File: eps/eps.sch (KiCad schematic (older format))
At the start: 64 parts, among them Q1 IRF7404, Q10 2N7002, Q11 IRF7404, Q12 2N7002, Q13 IRF7404, Q14 2N7002, Q15 IRF7404, Q16 IRF7404, Q17 IRF7404, Q18 IRF7404, Q19 IRF7404, Q2 2N7002, Q20 2N7002, Q21 IRF7404, Q22 2N7002, Q23 IRF7404, Q24 2N7002, Q3 IRF7404, Q4 2N7002, Q5 IRF7404, Q6 2N7002, Q7 IRF7404, Q8 2N7002, Q9 IRF7404

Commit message: switching regs
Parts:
- added U?: ADP2303ARDZ-3.3, Package_SO:SOIC-8-1EP_3.9x4.9mm_P1.27mm_EP2.29x3mm, symbol Regulator_Switching:ADP2303ARDZ-3.3
- added U?: ADP2303ARDZ-5.0, Package_SO:SOIC-8-1EP_3.9x4.9mm_P1.27mm_EP2.29x3mm, symbol Regulator_Switching:ADP2303ARDZ-5.0
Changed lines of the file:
@@
+	1    0    0    -1
+$EndComp
+$Comp
+L Regulator_Switching:ADP2303ARDZ-3.3 U?
+U 1 1 61773BE3
+P 6700 4800
+F 0 "U?" H 6700 5267 50  0000 C CNN
+F 1 "ADP2303ARDZ-3.3" H 6700 5176 50  0000 C CNN
+F 2 "Package_SO:SOIC-8-1EP_3.9x4.9mm_P1.27mm_EP2.29x3mm" H 6850 4450 50  0001 L CNN
+F 3 "https://www.analog.com/media/en/technical-documentation/data-sheets/ADP2302_2303.pdf" H 6500 5400 50  0001 C CNN
+	1    6700 4800
+	1    0    0    -1
+$EndComp
+$Comp
+L Regulator_Switching:ADP2303ARDZ-5.0 U?
+U 1 1 61775A47
+P 8750 4900
+F 0 "U?" H 8750 5367 50  0000 C CNN
+F 1 "ADP2303ARDZ-5.0" H 8750 5276 50  0000 C CNN
+F 2 "Package_SO:SOIC-8-1EP_3.9x4.9mm_P1.27mm_EP2.29x3mm" H 8900 4550 50  0001 L CNN
+F 3 "https://www.analog.com/media/en/technical-documentation/data-sheets/ADP2302_2303.pdf" H 8550 5500 50  0001 C CNN
+	1    8750 4900
 	1    0    0    -1
 $EndComp

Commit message: switching regulators
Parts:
- removed U?: ADP2303ARDZ-3.3, Package_SO:SOIC-8-1EP_3.9x4.9mm_P1.27mm_EP2.29x3mm, symbol Regulator_Switching:ADP2303ARDZ-3.3
- added U1: ADP2302ARDZ-3.3, Package_SO:SOIC-8-1EP_3.9x4.9mm_P1.27mm_EP2.29x3mm, symbol Regulator_Switching:ADP2302ARDZ-3.3
- added U3: CS5172EDR8G, symbol epslib:CS5172EDR8G
- gave numbers to parts that had none: 1
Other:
- moved on the sheet: U2
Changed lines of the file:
@@
 	1700 4200 2500 4200
 $Comp
-L power:GND #PWR?
+L power:GND #PWR0101
 U 1 1 617757AB
 P 2500 4200
-F 0 "#PWR?" H 2500 3950 50  0001 C CNN
+F 0 "#PWR0101" H 2500 3950 50  0001 C CNN
 F 1 "GND" H 2505 4027 50  0000 C CNN
 F 2 "" H 2500 4200 50  0001 C CNN
@@
 BUS12SIG
 $Comp
-L power:+12V #PWR?
+L power:+12V #PWR0102
 U 1 1 61798D3E
 P 9450 2900
-F 0 "#PWR?" H 9450 2750 50  0001 C CNN
+F 0 "#PWR0102" H 9450 2750 50  0001 C CNN
 F 1 "+12V" V 9465 3028 50  0000 L CNN
 F 2 "" H 9450 2900 50  0001 C CNN
@@
 $EndComp
 $Comp
-L power:+3.3V #PWR?
+L power:+3.3V #PWR0103
 U 1 1 6179B4E0
 P 4800 2900
-F 0 "#PWR?" H 4800 2750 50  0001 C CNN
+F 0 "#PWR0103" H 4800 2750 50  0001 C CNN
 F 1 "+3.3V" V 4815 3028 50  0000 L CNN
 F 2 "" H 4800 2900 50  0001 C CNN
@@
 $EndComp
 $Comp
-L power:+12V #PWR?
+L power:+12V #PWR0104
 U 1 1 6179E69D
 P 4800 800
-F 0 "#PWR?" H 4800 650 50  0001 C CNN
+F 0 "#PWR0104" H 4800 650 50  0001 C CNN
 F 1 "+12V" V 4815 928 50  0000 L CNN
 F 2 "" H 4800 800 50  0001 C CNN
@@
 BUSBSIG
 $Comp
-L power:+3.3V #PWR?
+L power:+3.3V #PWR0105
 U 1 1 617A7227
 P 7900 1850
-F 0 "#PWR?" H 7900 1700 50  0001 C CNN
+F 0 "#PWR0105" H 7900 1700 50  0001 C CNN
 F 1 "+3.3V" V 7915 1978 50  0000 L CNN
 F 2 "" H 7900 1850 50  0001 C CNN
@@
 $EndComp
 $Comp
-L power:+BATT #PWR?
+L power:+BATT #PWR0106
 U 1 1 617A95E4
 P 7900 2900
-F 0 "#PWR?" H 7900 2750 50  0001 C CNN
+F 0 "#PWR0106" H 7900 2750 50  0001 C CNN
 F 1 "+BATT" H 7915 3073 50  0000 C CNN
 F 2 "" H 7900 2900 50  0001 C CNN
@@
 	4350 800  4800 800
 $Comp
-L power:GND #PWR?
+L power:GND #PWR0107
 U 1 1 617E29A2
 P 4350 1600
-F 0 "#PWR?" H 4350 1350 50  0001 C CNN
+F 0 "#PWR0107" H 4350 1350 50  0001 C CNN
 F 1 "GND" H 4355 1427 50  0000 C CNN
 F 2 "" H 4350 1600 50  0001 C CNN
@@
 SIG2
 $Comp
-L power:+12V #PWR?
+L power:+12V #PWR0108
 U 1 1 617F4B03
 P 6350 800
-F 0 "#PWR?" H 6350 650 50  0001 C CNN
+F 0 "#PWR0108" H 6350 650 50  0001 C CNN
 F 1 "+12V" V 6365 928 50  0000 L CNN
 F 2 "" H 6350 800 50  0001 C CNN
@@
 	5900 800  6350 800
 $Comp
-L power:GND #PWR?
+L power:GND #PWR0109
 U 1 1 617F4B27
 P 5900 1600
-F 0 "#PWR?" H 5900 1350 50  0001 C CNN
+F 0 "#PWR0109" H 5900 1350 50  0001 C CNN
 F 1 "GND" H 5905 1427 50  0000 C CNN
 F 2 "" H 5900 1600 50  0001 C CNN
@@
 	7450 800  7900 800
 $Comp
-L power:GND #PWR?
+L power:GND #PWR0110
 U 1 1 6180AD18
 P 7450 1600
-F 0 "#PWR?" H 7450 1350 50  0001 C CNN
+F 0 "#PWR0110" H 7450 1350 50  0001 C CNN
 F 1 "GND" H 7455 1427 50  0000 C CNN
 F 2 "" H 7450 1600 50  0001 C CNN
@@
 	7100 1300 7150 1300
 $Comp
-L power:+BATT #PWR?
+L power:+BATT #PWR0111
 U 1 1 6180E8E3
 P 7900 800
-F 0 "#PWR?" H 7900 650 50  0001 C CNN
+F 0 "#PWR0111" H 7900 650 50  0001 C CNN
 F 1 "+BATT" H 7915 973 50  0000 C CNN
 F 2 "" H 7900 800 50  0001 C CNN
@@
 	9000 800  9450 800
 $Comp
-L power:GND #PWR?
+L power:GND #PWR0112
 U 1 1 6182C3CE
 P 9000 1600
-F 0 "#PWR?" H 9000 1350 50  0001 C CNN
+F 0 "#PWR0112" H 9000 1350 50  0001 C CNN
 F 1 "GND" H 9005 1427 50  0000 C CNN
 F 2 "" H 9000 1600 50  0001 C CNN
@@
 	8650 1300 8700 1300
 $Comp
-L power:+BATT #PWR?
+L power:+BATT #PWR0113
 U 1 1 6182C3E0
 P 9450 800
-F 0 "#PWR?" H 9450 650 50  0001 C CNN
+F 0 "#PWR0113" H 9450 650 50  0001 C CNN
 F 1 "+BATT" H 9465 973 50  0000 C CNN
 F 2 "" H 9450 800 50  0001 C CNN
@@
 	10550 800  11000 800
 $Comp
-L power:GND #PWR?
+L power:GND #PWR0114
 U 1 1 61857DDD
 P 10550 1600
-F 0 "#PWR?" H 10550 1350 50  0001 C CNN
+F 0 "#PWR0114" H 10550 1350 50  0001 C CNN
 F 1 "GND" H 10555 1427 50  0000 C CNN
 F 2 "" H 10550 1600 50  0001 C CNN
@@
 	10200 1300 10250 1300
 $Comp
-L power:+5V #PWR?
+L power:+5V #PWR0115
 U 1 1 6185C627
 P 11000 800
-F 0 "#PWR?" H 11000 650 50  0001 C CNN
+F 0 "#PWR0115" H 11000 650 50  0001 C CNN
 F 1 "+5V" V 11015 928 50  0000 L CNN
 F 2 "" H 11000 800 50  0001 C CNN
@@
 	4350 1850 4800 1850
 $Comp
-L power:GND #PWR?
+L power:GND #PWR0116
 U 1 1 61868CA2
 P 4350 2650
-F 0 "#PWR?" H 4350 2400 50  0001 C CNN
+F 0 "#PWR0116" H 4350 2400 50  0001 C CNN
 F 1 "GND" H 4355 2477 50  0000 C CNN
 F 2 "" H 4350 2650 50  0001 C CNN
@@
 	4000 2350 4050 2350
 $Comp
-L power:+5V #PWR?
+L power:+5V #PWR0117
 U 1 1 61868CB4
 P 4800 1850
-F 0 "#PWR?" H 4800 1700 50  0001 C CNN
+F 0 "#PWR0117" H 4800 1700 50  0001 C CNN
 F 1 "+5V" V 4815 1978 50  0000 L CNN
 F 2 "" H 4800 1850 50  0001 C CNN
@@
 	5900 1850 6350 1850
 $Comp
-L power:GND #PWR?
+L power:GND #PWR0118
 U 1 1 61889281
 P 5900 2650
-F 0 "#PWR?" H 5900 2400 50  0001 C CNN
+F 0 "#PWR0118" H 5900 2400 50  0001 C CNN
 F 1 "GND" H 5905 2477 50  0000 C CNN
 F 2 "" H 5900 2650 50  0001 C CNN
@@
 	5550 2350 5600 2350
 $Comp
-L power:+5V #PWR?
+L power:+5V #PWR0119
 U 1 1 61889293
 P 6350 1850
-F 0 "#PWR?" H 6350 1700 50  0001 C CNN
+F 0 "#PWR0119" H 6350 1700 50  0001 C CNN
 F 1 "+5V" V 6365 1978 50  0000 L CNN
 F 2 "" H 6350 1850 50  0001 C CNN
@@
 Connection ~ 7900 1850
 $Comp
-L power:+3.3V #PWR?
+L power:+3.3V #PWR0120
 U 1 1 618CA6F8
 P 9450 1850
-F 0 "#PWR?" H 9450 1700 50  0001 C CNN
+F 0 "#PWR0120" H 9450 1700 50  0001 C CNN
 F 1 "+3.3V" V 9465 1978 50  0000 L CNN
 F 2 "" H 9450 1850 50  0001 C CNN
@@
 SIG10
 $Comp
-L power:+3.3V #PWR?
+L power:+3.3V #PWR0121
 U 1 1 618DDDFA
 P 11000 1850
-F 0 "#PWR?" H 11000 1700 50  0001 C CNN
+F 0 "#PWR0121" H 11000 1700 50  0001 C CNN
 F 1 "+3.3V" V 11015 1978 50  0000 L CNN
 F 2 "" H 11000 1850 50  0001 C CNN
@@
 	5900 2900 6350 2900
 $Comp
-L power:GND #PWR?
+L power:GND #PWR0122
 U 1 1 61926FFE
 P 5900 3700
-F 0 "#PWR?" H 5900 3450 50  0001 C CNN
+F 0 "#PWR0122" H 5900 3450 50  0001 C CNN
 F 1 "GND" H 5905 3527 50  0000 C CNN
 F 2 "" H 5900 3700 50  0001 C CNN
@@
 	5550 3400 5600 3400
 $Comp
-L power:+5V #PWR?
+L power:+5V #PWR0123
 U 1 1 61927010
 P 6350 2900
-F 0 "#PWR?" H 6350 2750 50  0001 C CNN
+F 0 "#PWR0123" H 6350 2750 50  0001 C CNN
 F 1 "+5V" V 6365 3028 50  0000 L CNN
 F 2 "" H 6350 2900 50  0001 C CNN
@@
 	7450 2900 7900 2900
 $Comp
-L power:GND #PWR?
+L power:GND #PWR0124
 U 1 1 6193C01F
 P 7450 3700
-F 0 "#PWR?" H 7450 3450 50  0001 C CNN
+F 0 "#PWR0124" H 7450 3450 50  0001 C CNN
 F 1 "GND" H 7455 3527 50  0000 C CNN
 F 2 "" H 7450 3700 50  0001 C CNN
@@
 	9000 2900 9450 2900
 $Comp
-L power:GND #PWR?
+L power:GND #PWR0125
 U 1 1 61959DFB
 P 9000 3700
-F 0 "#PWR?" H 9000 3450 50  0001 C CNN
+F 0 "#PWR0125" H 9000 3450 50  0001 C CNN
 F 1 "GND" H 9005 3527 50  0000 C CNN
 F 2 "" H 9000 3700 50  0001 C CNN
@@
 Connection ~ 9450 2900
 $Comp
-L power:GND #PWR?
+L power:GND #PWR0126
 U 1 1 6176AAEA
 P 4450 3500
-F 0 "#PWR?" H 4450 3250 50  0001 C CNN
+F 0 "#PWR0126" H 4450 3250 50  0001 C CNN
 F 1 "GND" H 4455 3327 50  0000 C CNN
 F 2 "" H 4450 3500 50  0001 C CNN
@@
 $EndComp
 $Comp
-L power:+3.3V #PWR?
+L power:+3.3V #PWR0127
 U 1 1 6178C4CA
 P 5550 3100
-F 0 "#PWR?" H 5550 2950 50  0001 C CNN
+F 0 "#PWR0127" H 5550 2950 50  0001 C CNN
 F 1 "+3.3V" H 5565 3273 50  0000 C CNN
 F 2 "" H 5550 3100 50  0001 C CNN
@@
 $EndComp
 $Comp
-L power:+3.3V #PWR?
+L power:+3.3V #PWR0128
 U 1 1 6178CD8E
 P 7100 3100
-F 0 "#PWR?" H 7100 2950 50  0001 C CNN
+F 0 "#PWR0128" H 7100 2950 50  0001 C CNN
 F 1 "+3.3V" H 7115 3273 50  0000 C CNN
 F 2 "" H 7100 3100 50  0001 C CNN
@@
 $EndComp
 $Comp
-L power:+3.3V #PWR?
+L power:+3.3V #PWR0129
 U 1 1 61790B8A
 P 8650 3100
-F 0 "#PWR?" H 8650 2950 50  0001 C CNN
+F 0 "#PWR0129" H 8650 2950 50  0001 C CNN
 F 1 "+3.3V" H 8665 3273 50  0000 C CNN
 F 2 "" H 8650 3100 50  0001 C CNN
@@
 $EndComp
 $Comp
-L Regulator_Switching:ADP2303ARDZ-3.3 U?
-U 1 1 61773BE3
-P 6700 4800
-F 0 "U?" H 6700 5267 50  0000 C CNN
-F 1 "ADP2303ARDZ-3.3" H 6700 5176 50  0000 C CNN
-F 2 "Package_SO:SOIC-8-1EP_3.9x4.9mm_P1.27mm_EP2.29x3mm" H 6850 4450 50  0001 L CNN
-F 3 "https://www.analog.com/media/en/technical-documentation/data-sheets/ADP2302_2303.pdf" H 6500 5400 50  0001 C CNN
-	1    6700 4800
-	1    0    0    -1
-$EndComp
-$Comp
-L Regulator_Switching:ADP2303ARDZ-5.0 U?
+L Regulator_Switching:ADP2303ARDZ-5.0 U2
 U 1 1 61775A47
-P 8750 4900
-F 0 "U?" H 8750 5367 50  0000 C CNN
-F 1 "ADP2303ARDZ-5.0" H 8750 5276 50  0000 C CNN
-F 2 "Package_SO:SOIC-8-1EP_3.9x4.9mm_P1.27mm_EP2.29x3mm" H 8900 4550 50  0001 L CNN
-F 3 "https://www.analog.com/media/en/technical-documentation/data-sheets/ADP2302_2303.pdf" H 8550 5500 50  0001 C CNN
-	1    8750 4900
-	1    0    0    -1
-$EndComp
+P 8750 4850
+F 0 "U2" H 8750 5317 50  0000 C CNN
+F 1 "ADP2303ARDZ-5.0" H 8750 5226 50  0000 C CNN
+F 2 "Package_SO:SOIC-8-1EP_3.9x4.9mm_P1.27mm_EP2.29x3mm" H 8900 4500 50  0001 L CNN
+F 3 "https://www.analog.com/media/en/technical-documentation/data-sheets/ADP2302_2303.pdf" H 8550 5450 50  0001 C CNN
+	1    8750 4850
+	1    0    0    -1
+$EndComp
+$Comp
+L Regulator_Switching:ADP2302ARDZ-3.3 U1
+U 1 1 6178A820
+P 7300 4850
+F 0 "U1" H 7300 5317 50  0000 C CNN
+F 1 "ADP2302ARDZ-3.3" H 7300 5226 50  0000 C CNN
+F 2 "Package_SO:SOIC-8-1EP_3.9x4.9mm_P1.27mm_EP2.29x3mm" H 7450 4500 50  0001 L CNN
+F 3 "https://www.analog.com/media/en/technical-documentation/data-sheets/ADP2302_2303.pdf" H 7100 5450 50  0001 C CNN
+	1    7300 4850
+	1    0    0    -1
+$EndComp
+$Comp
+L epslib:CS5172EDR8G U3
+U 1 1 6178D5F2
+P 5800 4550
+F 0 "U3" H 5800 4675 50  0000 C CNN
+F 1 "CS5172EDR8G" H 5800 4584 50  0000 C CNN
+F 2 "" H 5800 4550 50  0001 C CNN
+F 3 "" H 5800 4550 50  0001 C CNN
+	1    5800 4550
+	1    0    0    -1
+$EndComp

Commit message: organization
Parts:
- removed Q1, Q11, Q13, Q15, Q16, Q17, Q18, Q19, Q21, Q23, Q3, Q5, Q7, Q9: IRF7404, Package_SO:SOIC-8_3.9x4.9mm_P1.27mm, symbol Transistor_FET:IRF7404
- removed Q10, Q12, Q14, Q2, Q20, Q22, Q24, Q4, Q6, Q8: 2N7002, Package_TO_SOT_SMD:SOT-23, symbol Transistor_FET:2N7002
- removed R1, R10, R13, R16, R19, R22, R24, R26, R28, R30, R33, R36, R4, R7: 100R, symbol Device:R
- removed R11, R12, R14, R15, R17, R18, R2, R20, R21, R23, R25, R27, R29, R3, R31, R32, R34, R35, R37, R38, R5, R6, R8, R9: 10K, symbol Device:R
- removed U1: ADP2302ARDZ-3.3, Package_SO:SOIC-8-1EP_3.9x4.9mm_P1.27mm_EP2.29x3mm, symbol Regulator_Switching:ADP2302ARDZ-3.3
- removed U2: ADP2303ARDZ-5.0, Package_SO:SOIC-8-1EP_3.9x4.9mm_P1.27mm_EP2.29x3mm, symbol Regulator_Switching:ADP2303ARDZ-5.0
- removed U3: CS5172EDR8G, symbol epslib:CS5172EDR8G
- added U4: STM32F411CEUx, Package_DFN_QFN:QFN-48-1EP_7x7mm_P0.5mm_EP5.6x5.6mm, symbol MCU_ST_STM32F4:STM32F411CEUx
- added U?: LTC4365TS8, symbol Power_Management:LTC4365TS8
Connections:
- net 12VBUS is gone; now on net +12V: H2.23 (Pin_23), H2.24 (Pin_24)
- net 3V3BUS is gone; now on net +3V3: H2.27 (Pin_27), H2.28 (Pin_28)
- net 5VBUS is gone; now on net +5V: H2.25 (Pin_25), H2.26 (Pin_26)
- net BATTBUS is gone; now on net +BATT: H2.45 (Pin_45), H2.46 (Pin_46)
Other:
- note added: "Distributes bus powers to PDM outputs. \nReads PDM telemetry\n"
- note added: "Regulates BatV to 3.3V, 5V, 12V buses\nIncludes OCP/UVP and resets\nReads bus telemetry"
- note added: "Regulates solar panel voltage\nReads telemetry from panels\n"
- note removed: "TWENTY-FOUR MOSFETS!!!!!"

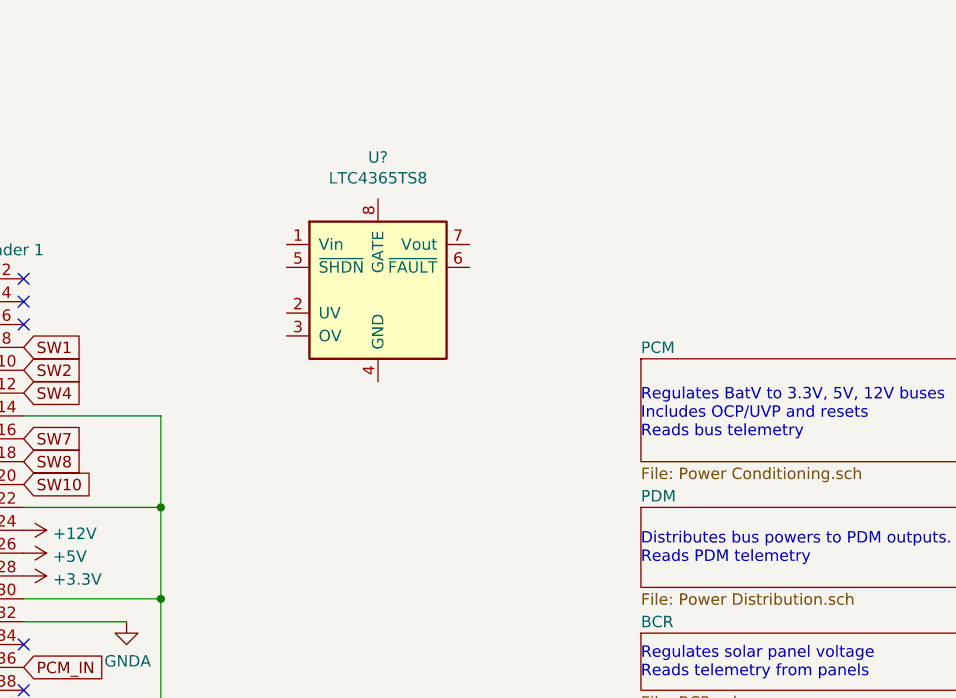
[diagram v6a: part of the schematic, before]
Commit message: implement uvp/ovp
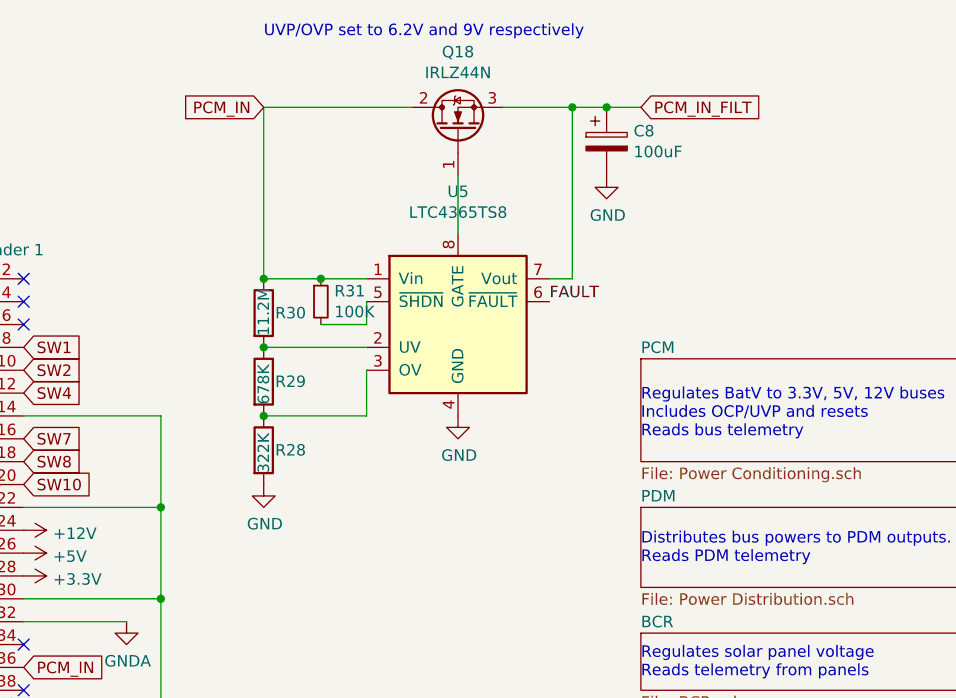
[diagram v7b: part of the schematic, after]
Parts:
- added C8: 100uF, symbol Device:CP
- added Q18: IRLZ44N, Package_TO_SOT_THT:TO-220-3_Vertical, symbol Transistor_FET:IRLZ44N
- added R28: 322K, symbol Device:R
- added R29: 678K, symbol Device:R
- added R30: 11.2M, symbol Device:R
- added R31: 100K, symbol Device:R_Small
- gave numbers to parts that had none: 1
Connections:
- net GND: now also U5.4 (GND), C8.2, R28.2
- net PCM_IN: now also U5.1 (Vin), Q18.2 (D), R30.1, R31.1
- net at U5.2 (UV): now also R29.1, R30.2
- net at U5.3 (OV): now also R28.1, R29.2
- net at U5.5 (~SHDN): now also R31.2
- net FAULT: now reaches U5.6 (~FAULT)
- net PCM_IN_FILT: now reaches U5.7 (Vout)
- net PCM_IN_FILT: now also C8.1, Q18.3 (S)
- net at U5.8 (GATE): now also Q18.1 (G)
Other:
- note added: "UVP/OVP set to 6.2V and 9V respectively"
- moved on the sheet: U5
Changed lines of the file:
@@
 $EndComp
 $Comp
-L Power_Management:LTC4365TS8 U?
+L Power_Management:LTC4365TS8 U5
 U 1 1 6180BC68
-P 4300 1700
-F 0 "U?" H 4300 2281 50  0000 C CNN
-F 1 "LTC4365TS8" H 4300 2190 50  0000 C CNN
-F 2 "" H 4000 1950 50  0001 C CNN
-F 3 "https://www.analog.com/media/en/technical-documentation/data-sheets/4365fa.pdf" H 4300 1800 50  0001 C CNN
-	1    4300 1700
+P 4650 1850
+F 0 "U5" H 4650 2431 50  0000 C CNN
+F 1 "LTC4365TS8" H 4650 2340 50  0000 C CNN
+F 2 "" H 4350 2100 50  0001 C CNN
+F 3 "https://www.analog.com/media/en/technical-documentation/data-sheets/4365fa.pdf" H 4650 1950 50  0001 C CNN
+	1    4650 1850
 	1    0    0    -1
 $EndComp
+$Comp
+L Transistor_FET:IRLZ44N Q18
+U 1 1 6180D601
+P 4650 1000
+F 0 "Q18" V 4992 1000 50  0000 C CNN
+F 1 "IRLZ44N" V 4901 1000 50  0000 C CNN
+F 2 "Package_TO_SOT_THT:TO-220-3_Vertical" H 4900 925 50  0001 L CIN
+F 3 "http://www.irf.com/product-info/datasheets/data/irlz44n.pdf" H 4650 1000 50  0001 L CNN
+	1    4650 1000
+	0    -1   -1   0
+$EndComp
+Wire Wire Line
+	4650 1450 4650 1200
+Text GLabel 3800 900  0    50   Input ~ 0
+PCM_IN
+Wire Wire Line
+	3800 1650 3800 900
+Wire Wire Line
+	4850 900  5150 900
+Wire Wire Line
+	5050 1650 5150 1650
+Wire Wire Line
+	5150 1650 5150 900
+Text GLabel 5450 900  2    50   Input ~ 0
+PCM_IN_FILT
+Wire Wire Line
+	5150 900  5300 900
+Connection ~ 5150 900
+$Comp
+L Device:CP C8
+U 1 1 618175DC
+P 5300 1050
+F 0 "C8" H 5418 1096 50  0000 L CNN
+F 1 "100uF" H 5418 1005 50  0000 L CNN
+F 2 "" H 5338 900 50  0001 C CNN
+F 3 "~" H 5300 1050 50  0001 C CNN
+	1    5300 1050
+	1    0    0    -1
+$EndComp
+Connection ~ 5300 900
+Wire Wire Line
+	5300 900  5450 900
+$Comp
+L power:GND #PWR033
+U 1 1 6181B18B
+P 5300 1200
+F 0 "#PWR033" H 5300 950 50  0001 C CNN
+F 1 "GND" H 5305 1027 50  0000 C CNN
+F 2 "" H 5300 1200 50  0001 C CNN
+F 3 "" H 5300 1200 50  0001 C CNN
+	1    5300 1200
+	1    0    0    -1
+$EndComp
+$Comp
+L Device:R R28
+U 1 1 6181BFCB
+P 3800 2400
+F 0 "R28" H 3850 2400 50  0000 L CNN
+F 1 "322K" V 3800 2300 50  0000 L CNN
+F 2 "" V 3730 2400 50  0001 C CNN
+F 3 "~" H 3800 2400 50  0001 C CNN
+	1    3800 2400
+	1    0    0    -1
+$EndComp
+$Comp
+L Device:R R29
+U 1 1 6181C3B8
+P 3800 2100
+F 0 "R29" H 3850 2100 50  0000 L CNN
+F 1 "678K" V 3800 2000 50  0000 L CNN
+F 2 "" V 3730 2100 50  0001 C CNN
+F 3 "~" H 3800 2100 50  0001 C CNN
+	1    3800 2100
+	1    0    0    -1
+$EndComp
+$Comp
+L Device:R R30
+U 1 1 6181CB56
+P 3800 1800
+F 0 "R30" H 3850 1800 50  0000 L CNN
+F 1 "11.2M" V 3800 1700 50  0000 L CNN
+F 2 "" V 3730 1800 50  0001 C CNN
+F 3 "~" H 3800 1800 50  0001 C CNN
+	1    3800 1800
+	1    0    0    -1
+$EndComp
+Wire Wire Line
+	4250 2050 4250 2250
+$Comp
+L Device:R_Small R31
+U 1 1 6181F3F7
+P 4050 1750
+F 0 "R31" H 4109 1796 50  0000 L CNN
+F 1 "100K" H 4109 1705 50  0000 L CNN
+F 2 "" H 4050 1750 50  0001 C CNN
+F 3 "~" H 4050 1750 50  0001 C CNN
+	1    4050 1750
+	1    0    0    -1
+$EndComp
+Wire Wire Line
+	3800 900  4450 900
+Connection ~ 4050 1650
+Wire Wire Line
+	4050 1650 4250 1650
+Wire Wire Line
+	4250 1750 4250 1850
+Wire Wire Line
+	4250 1850 4050 1850
+Wire Wire Line
+	3800 1650 4050 1650
+Connection ~ 3800 1650
+Wire Wire Line
+	3800 1950 4250 1950
+Connection ~ 3800 1950
+Wire Wire Line
+	3800 2250 4250 2250
+Connection ~ 3800 2250
+$Comp
+L power:GND #PWR?
+U 1 1 61826AE0
+P 4650 2250
+F 0 "#PWR?" H 4650 2000 50  0001 C CNN
+F 1 "GND" H 4655 2077 50  0000 C CNN
+F 2 "" H 4650 2250 50  0001 C CNN
+F 3 "" H 4650 2250 50  0001 C CNN
+	1    4650 2250
+	1    0    0    -1
+$EndComp
+$Comp
+L power:GND #PWR?
+U 1 1 618271F0
+P 3800 2550
+F 0 "#PWR?" H 3800 2300 50  0001 C CNN
+F 1 "GND" H 3805 2377 50  0000 C CNN
+F 2 "" H 3800 2550 50  0001 C CNN
+F 3 "" H 3800 2550 50  0001 C CNN
+	1    3800 2550
+	1    0    0    -1
+$EndComp
+Text Label 5050 1750 0    50   ~ 0
+FAULT
+Text Notes 3800 600  0    50   ~ 0
+UVP/OVP set to 6.2V and 9V respectively
 $EndSCHEMATC
